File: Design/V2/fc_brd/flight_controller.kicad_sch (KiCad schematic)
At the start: 49 parts, among them U1 STM32H747BIT6, U2 W25Q128JVSIQ, U7 BMP390, U8 MMC5983MA, U9 BMI323

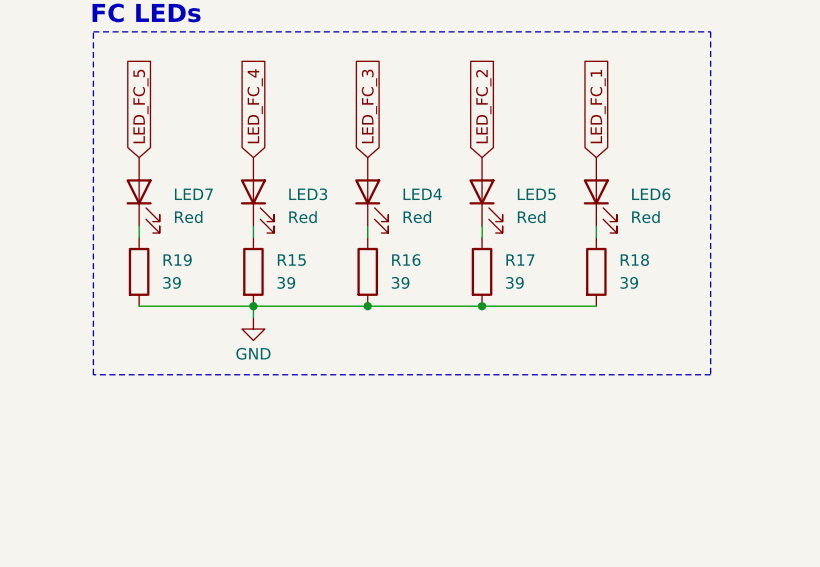
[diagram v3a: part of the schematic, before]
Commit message: VCORE is regulated with LDO instead of SMPS. Remove VCAP connection to 3.3V as VCAP is an output not an input
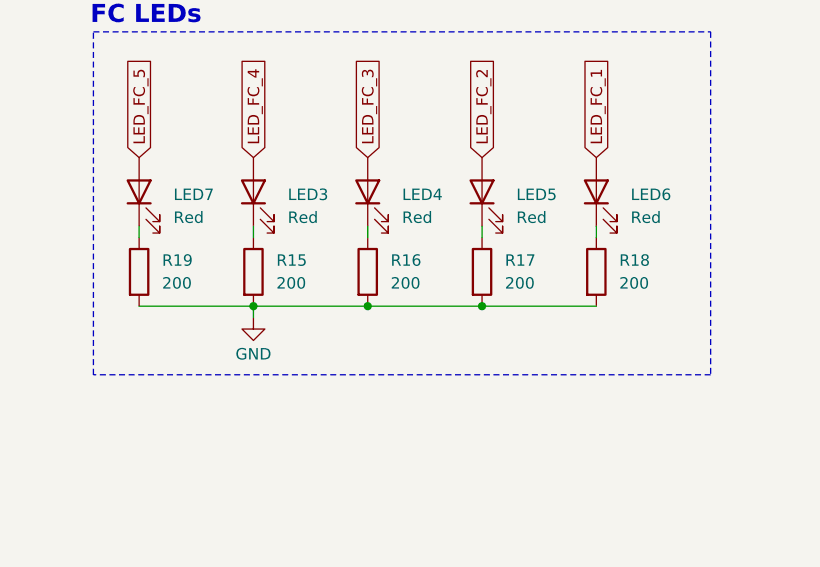
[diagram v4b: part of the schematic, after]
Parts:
- R15, R16, R17, R18, R19: value 39 -> 200; LCSC Part # C2907032 -> C8218; Manufacturer_Name FOJAN -> UNI-ROYAL(Uniroyal Elec); Manufacturer_Part_Number FRC0603F39R0TS -> 0603WAF2000T5E
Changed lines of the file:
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@@
 			)
 		)
-		(property "Value" "39"
+		(property "Value" "200"
 			(at 243.84 308.6099 0)
 			(effects
@@
 			)
 		)
-		(property "Description" "330 Ohms ±1% 0.25W, 1/4W Chip Resistor 0603 (1608 Metric) Automotive AEC-Q200, Pulse Withstanding Thick Film"
+		(property "Description" "-55℃~+155℃ 100mW 200Ω 75V Thick Film Resistor ±1% ±100ppm/℃ 0603 Chip Resistor - Surface Mount ROHS"
 			(at 241.3 307.34 0)
 			(effects
@@
 			)
 		)
-		(property "Manufacturer_Name" "FOJAN"
+		(property "Manufacturer_Name" "UNI-ROYAL(Uniroyal Elec)"
 			(at 241.3 307.34 0)
 			(effects
@@
 			)
 		)
-		(property "Manufacturer_Part_Number" "FRC0603F39R0TS"
+		(property "Manufacturer_Part_Number" "0603WAF2000T5E"
 			(at 241.3 307.34 0)
 			(effects
@@
 			)
 		)
-		(property "LCSC Part #" "C2907032"
+		(property "LCSC Part #" "C8218"
 			(at 241.3 307.34 0)
 			(effects
@@
 			)
 		)
-		(property "Value" "39"
+		(property "Value" "200"
 			(at 281.94 308.6099 0)
 			(effects
@@
 			)
 		)
-		(property "Description" "330 Ohms ±1% 0.25W, 1/4W Chip Resistor 0603 (1608 Metric) Automotive AEC-Q200, Pulse Withstanding Thick Film"
+		(property "Description" "-55℃~+155℃ 100mW 200Ω 75V Thick Film Resistor ±1% ±100ppm/℃ 0603 Chip Resistor - Surface Mount ROHS"
 			(at 279.4 307.34 0)
 			(effects
@@
 			)
 		)
-		(property "Manufacturer_Name" "FOJAN"
+		(property "Manufacturer_Name" "UNI-ROYAL(Uniroyal Elec)"
 			(at 279.4 307.34 0)
 			(effects
@@
 			)
 		)
-		(property "Manufacturer_Part_Number" "FRC0603F39R0TS"
+		(property "Manufacturer_Part_Number" "0603WAF2000T5E"
 			(at 279.4 307.34 0)
 			(effects
@@
 			)
 		)
-		(property "LCSC Part #" "C2907032"
+		(property "LCSC Part #" "C8218"
 			(at 279.4 307.34 0)
 			(effects
@@
 			)
 		)
-		(property "Value" "39"
+		(property "Value" "200"
 			(at 269.24 308.6099 0)
 			(effects
@@
 			)
 		)
-		(property "Description" "330 Ohms ±1% 0.25W, 1/4W Chip Resistor 0603 (1608 Metric) Automotive AEC-Q200, Pulse Withstanding Thick Film"
+		(property "Description" "-55℃~+155℃ 100mW 200Ω 75V Thick Film Resistor ±1% ±100ppm/℃ 0603 Chip Resistor - Surface Mount ROHS"
 			(at 266.7 307.34 0)
 			(effects
@@
 			)
 		)
-		(property "Manufacturer_Name" "FOJAN"
+		(property "Manufacturer_Name" "UNI-ROYAL(Uniroyal Elec)"
 			(at 266.7 307.34 0)
 			(effects
@@
 			)
 		)
-		(property "Manufacturer_Part_Number" "FRC0603F39R0TS"
+		(property "Manufacturer_Part_Number" "0603WAF2000T5E"
 			(at 266.7 307.34 0)
 			(effects
@@
 			)
 		)
-		(property "LCSC Part #" "C2907032"
+		(property "LCSC Part #" "C8218"
 			(at 266.7 307.34 0)
 			(effects
@@
 			)
 		)
-		(property "Value" "39"
+		(property "Value" "200"
 			(at 294.64 308.6099 0)
 			(effects
@@
 			)
 		)
-		(property "Description" "330 Ohms ±1% 0.25W, 1/4W Chip Resistor 0603 (1608 Metric) Automotive AEC-Q200, Pulse Withstanding Thick Film"
+		(property "Description" "-55℃~+155℃ 100mW 200Ω 75V Thick Film Resistor ±1% ±100ppm/℃ 0603 Chip Resistor - Surface Mount ROHS"
 			(at 292.1 307.34 0)
 			(effects
@@
 			)
 		)
-		(property "Manufacturer_Name" "FOJAN"
+		(property "Manufacturer_Name" "UNI-ROYAL(Uniroyal Elec)"
 			(at 292.1 307.34 0)
 			(effects
@@
 			)
 		)
-		(property "Manufacturer_Part_Number" "FRC0603F39R0TS"
+		(property "Manufacturer_Part_Number" "0603WAF2000T5E"
 			(at 292.1 307.34 0)
 			(effects
@@
 			)
 		)
-		(property "LCSC Part #" "C2907032"
+		(property "LCSC Part #" "C8218"
 			(at 292.1 307.34 0)
 			(effects
@@
 			)
 		)
-		(property "Value" "39"
+		(property "Value" "200"
 			(at 256.54 308.6099 0)
 			(effects
@@
 			)
 		)
-		(property "Description" "330 Ohms ±1% 0.25W, 1/4W Chip Resistor 0603 (1608 Metric) Automotive AEC-Q200, Pulse Withstanding Thick Film"
+		(property "Description" "-55℃~+155℃ 100mW 200Ω 75V Thick Film Resistor ±1% ±100ppm/℃ 0603 Chip Resistor - Surface Mount ROHS"
 			(at 254 307.34 0)
 			(effects
@@
 			)
 		)
-		(property "Manufacturer_Name" "FOJAN"
+		(property "Manufacturer_Name" "UNI-ROYAL(Uniroyal Elec)"
 			(at 254 307.34 0)
 			(effects
@@
 			)
 		)
-		(property "Manufacturer_Part_Number" "FRC0603F39R0TS"
+		(property "Manufacturer_Part_Number" "0603WAF2000T5E"
 			(at 254 307.34 0)
 			(effects
@@
 			)
 		)
-		(property "LCSC Part #" "C2907032"
+		(property "LCSC Part #" "C8218"
 			(at 254 307.34 0)
 			(effects
